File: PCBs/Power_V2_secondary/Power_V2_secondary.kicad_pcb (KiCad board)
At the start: 2 copper layers, 50.1 x 84.3 mm, 9 parts, among them IC7 ACS712ELCTR-20A-T, J1 PCIE-164-02-F-D-TH-TR, J15 YK4420203000G, J8 Conn_01x02, U2 178.6164.0001

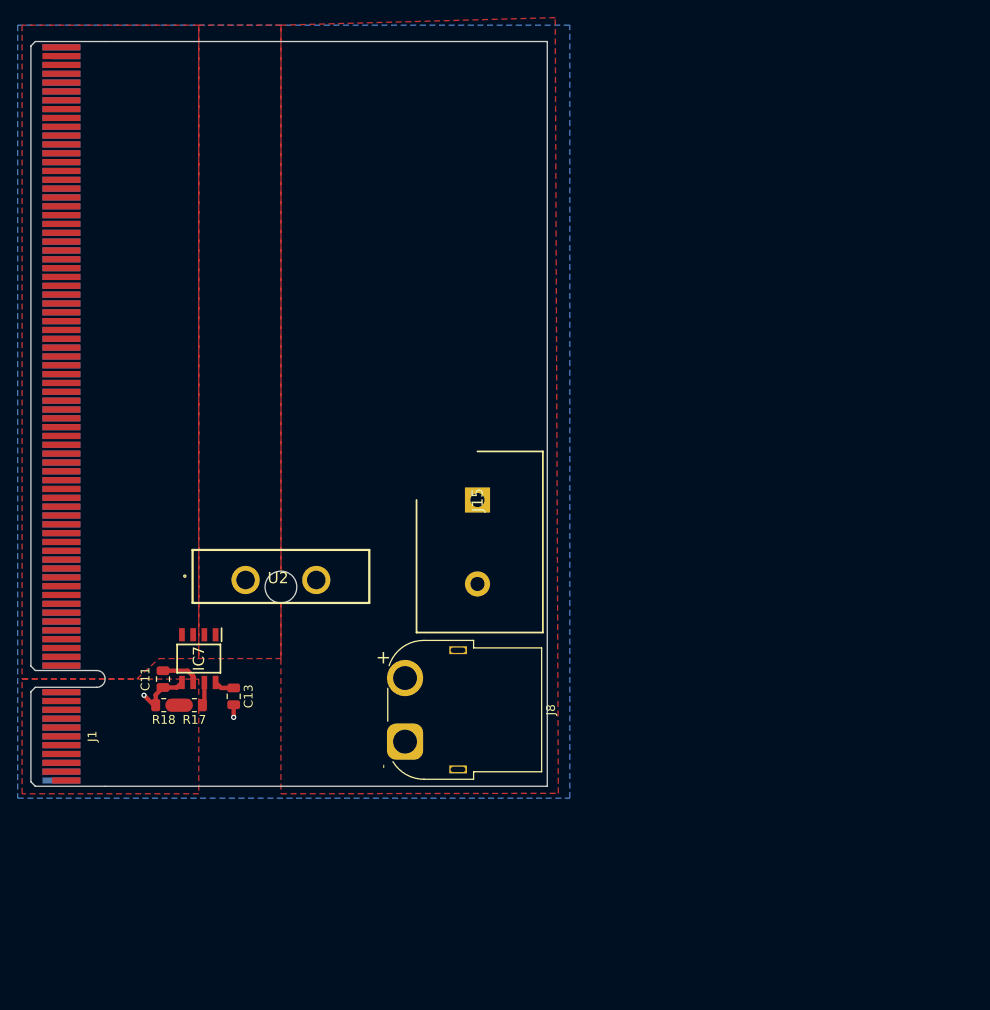
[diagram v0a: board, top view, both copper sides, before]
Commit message: finished secondary and beginning layout of main
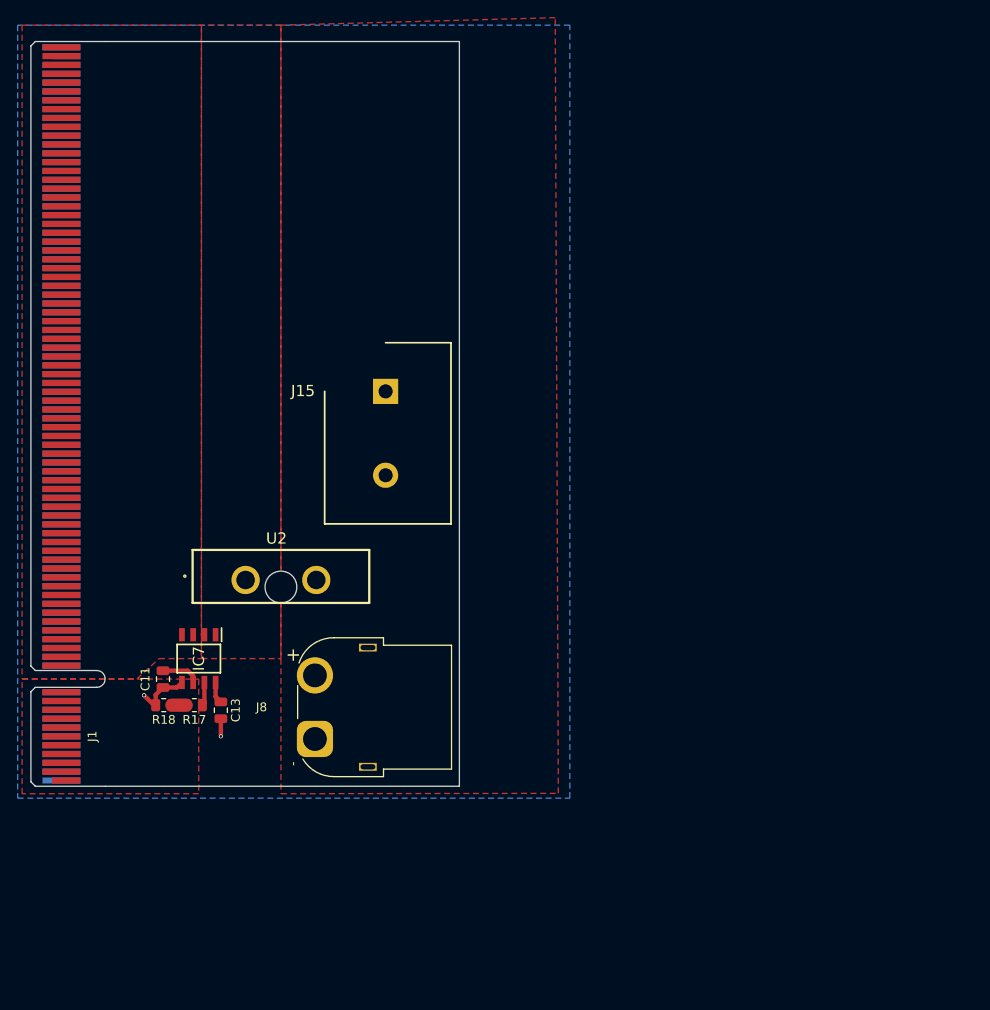
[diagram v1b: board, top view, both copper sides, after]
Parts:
- moved J15 16.1 mm to (81.7, 59.0)
- moved J8 10.2 mm to (73.7, 98.3)
- moved C13 2.14 mm to (63.0, 95.0)
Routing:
- net GND: track 7.94 -> 8.51 mm
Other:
- board size 50.1 x 84.3 mm -> 40.1 x 84.3 mm
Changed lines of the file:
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@@
 			(outputformat 1)
 			(mirror no)
-			(drillshape 1)
+			(drillshape 0)
 			(scaleselection 1)
-			(outputdirectory "")
+			(outputdirectory "./")
 		)
 	)
@@
 	(footprint "iprl_footprints:RHDR2W120P0X950_1X2_2050X1430X1790P"
 		(layer "F.Cu")
-		(at 92.05 71.25 -90)
+		(at 81.65 58.95 -90)
 		(descr "YK4420203000G")
 		(tags "Connector")
 		(property "Reference" "J15"
-			(at 0 0 90)
+			(at -0.05 9.35 0)
 			(layer "F.SilkS")
 			(effects
@@
 		)
 		(fp_text user "${REFERENCE}"
-			(at 0 0 90)
+			(at 0 9.35 0)
 			(layer "F.Fab")
 			(effects
@@
 		)
 		(embedded_fonts no)
-		(model "YK4420203000G.stp"
+		(model "/home/james/Documents/IPRL-Electronics-Hardware/PCBs/lib/models/YK4420203000G.stp"
 			(offset
 				(xyz 0 0 0)
@@
 	(footprint "Connector_AMASS:AMASS_XT60PW-F_1x02_P7.20mm_Horizontal"
 		(layer "F.Cu")
-		(at 83.85 98.6 -90)
+		(at 73.65 98.3 -90)
 		(descr "Connector XT60 Horizontal PCB Female, https://www.tme.eu/Document/1191bc2fa3aee3c446e5a895fd8f7983/XT60PW-F.pdf")
 		(tags "RC Connector XT60")
 		(property "Reference" "J8"
-			(at -3.6 -16.5 90)
+			(at -3.6 6.05 180)
 			(layer "F.SilkS")
 			(effects
@@
 	(footprint "Capacitor_SMD:C_0805_2012Metric"
 		(layer "F.Cu")
-		(at 64.45 93.47 -90)
+		(at 63 95.05 -90)
 		(descr "Capacitor SMD 0805 (2012 Metric), square (rectangular) end terminal, IPC-7351 nominal, (Body size source: IPC-SM-782 page 76, https://www.pcb-3d.com/wordpress/wp-content/uploads/ipc-sm-782a_amendment_1_and_2.pdf, https://docs.google.com/spreadsheets/d/1BsfQQcO9C6DZCsRaXUlFlo91Tg2WpOkGARC1WS5S8t0/edit?usp=sharing), generated with kicad-footprint-generator")
 		(tags "capacitor")
@@
 		(tags "Undefined or Miscellaneous")
 		(property "Reference" "U2"
-			(at -0.32439 -1.02275 0)
+			(at -0.5 -5.5 0)
 			(layer "F.SilkS")
 			(effects
@@
 		)
 		(fp_text user "${REFERENCE}"
-			(at -0.32439 -1.02275 0)
+			(at -0.4745 -5.5 0)
 			(layer "F.Fab")
 			(effects
@@
 		)
 		(embedded_fonts no)
-		(model "178.6164.0001.stp"
+		(model "${KIPRJMOD}/../lib/models/178.6164.0001.stp"
 			(offset
 				(xyz 4.999999925 10.31999954 -12.47000008)
@@
 		(tags "PCIe")
 		(property "Reference" "J1"
-			(at 5 3.5 -90)
+			(at 5 3.5 270)
 			(layer "F.SilkS")
 			(effects
@@
 		)
 		(property "Value" "PCIE-164-02-F-D-TH-TR"
-			(at 10.33 8.01 -90)
+			(at 10.33 8.01 270)
 			(layer "F.Fab")
 			(effects
@@
 		)
 		(fp_text user "${REFERENCE}"
-			(at 16 3.5 -90)
+			(at 16 3.5 270)
 			(layer "F.Fab")
 			(effects
@@
 	(gr_line
 		(start 49.9 103.65)
-		(end 99.95 103.65)
+		(end 90 103.65)
 		(stroke
 			(width 0.05)
@@
 	)
 	(gr_line
-		(start 99.95 103.65)
-		(end 99.95 19.35)
+		(start 90 103.65)
+		(end 90 19.35)
 		(stroke
 			(width 0.05)
@@
 	(gr_line
 		(start 49.9 19.35)
-		(end 99.95 19.35)
+		(end 90 19.35)
 		(stroke
 			(width 0.05)
@@
 	)
 	(segment
+		(start 63 96)
+		(end 63 98)
+		(width 0.5)
+		(layer "F.Cu")
+		(net 2)
+	)
+	(segment
 		(start 55.625 93.295)
 		(end 56.45 92.47)
@@
 		(net 2)
 	)
-	(segment
-		(start 64.45 94.42)
-		(end 64.45 95.85)
-		(width 0.5)
-		(layer "F.Cu")
-		(net 2)
-	)
 	(via
 		(at 54.3 93.35)
-		(size 0.6)
+		(size 0.45)
 		(drill 0.3)
 		(layers "F.Cu" "B.Cu")
@@
 	)
 	(via
-		(at 64.45 95.85)
-		(size 0.6)
+		(at 63 98)
+		(size 0.45)
 		(drill 0.3)
 		(layers "F.Cu" "B.Cu")
@@
 	)
 	(segment
-		(start 64.45 92.52)
-		(end 63.025 92.52)
+		(start 62.405 93.505)
+		(end 63 94.1)
 		(width 0.5)
 		(layer "F.Cu")
@@
 	)
 	(segment
-		(start 63.025 92.52)
-		(end 62.405 91.9)
+		(start 62.405 91.9)
+		(end 62.405 93.505)
 		(width 0.5)
 		(layer "F.Cu")
@@
 		(polygon
 			(pts
-				(xy 40.5 91.5) (xy 53.5 91.5) (xy 56 89.2) (xy 60.5 89.2) (xy 60.5 17.5) (xy 40.5 17.5)
+				(xy 40.5 91.5) (xy 53.5 91.5) (xy 56 89.2) (xy 60.8 89.2) (xy 60.8 17.5) (xy 40.5 17.5)
 			)
 		)
@@
 		(polygon
 			(pts
-				(xy 60.5 89.2) (xy 69.8 89.2) (xy 69.8 17.5) (xy 60.5 17.5)
+				(xy 60.8 89.2) (xy 69.8 89.2) (xy 69.8 17.5) (xy 60.8 17.5)
 			)
 		)
@@
 		(fill yes
 			(thermal_gap 0.5)
-			(thermal_bridge_width 0.5)
+			(thermal_bridge_width 1)
 		)
 		(polygon

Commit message: shortened main board and secondary
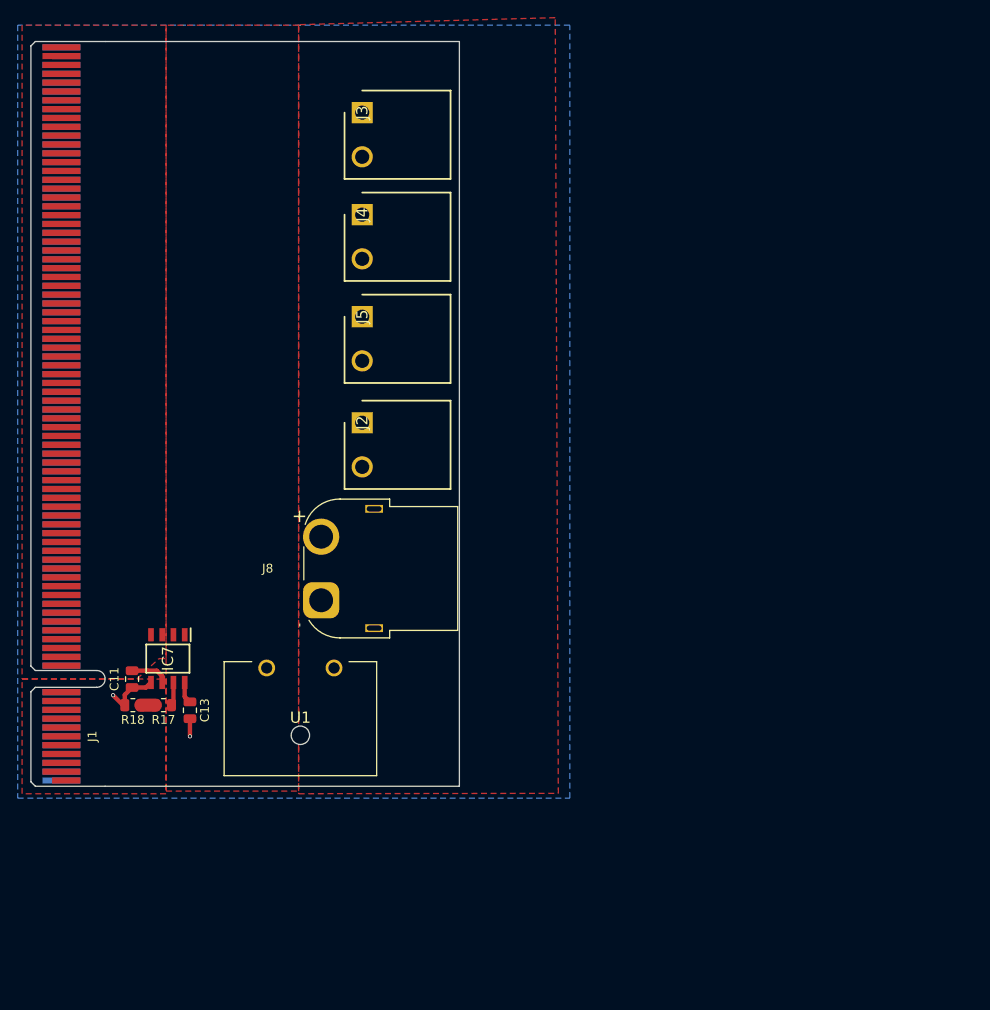
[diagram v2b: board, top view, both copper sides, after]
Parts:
- removed J15: YK4420203000G, iprl_footprints:RHDR2W120P0X950_1X2_2050X1430X1790P
- removed U2: 178.6164.0001, iprl_footprints:178.6164.XXX1
- added J2: 691312710002, iprl_footprints:SHDR2W100P0X500_1X2_1000X1200X850P, F.Cu at (79.0, 62.5)
- added J3: 691312710002, iprl_footprints:SHDR2W100P0X500_1X2_1000X1200X850P, F.Cu at (79.0, 27.4)
- added J4: 691312710002, iprl_footprints:SHDR2W100P0X500_1X2_1000X1200X850P, F.Cu at (79.0, 39.0)
- added J5: 691312710002, iprl_footprints:SHDR2W100P0X500_1X2_1000X1200X850P, F.Cu at (79.0, 50.5)
- added U1: 01530007Z, iprl_footprints:01530007Z, F.Cu at (72.0, 96.0)
- moved J8 15.7 mm to (74.3, 82.6)
- moved C11 3.50 mm to (53.0, 91.5)
- moved C13 3.50 mm to (59.5, 95.0)
- moved IC7 3.50 mm to (57.0, 89.2)
- moved R17 3.50 mm to (56.5, 94.5)
- moved R18 3.50 mm to (53.0, 94.5)

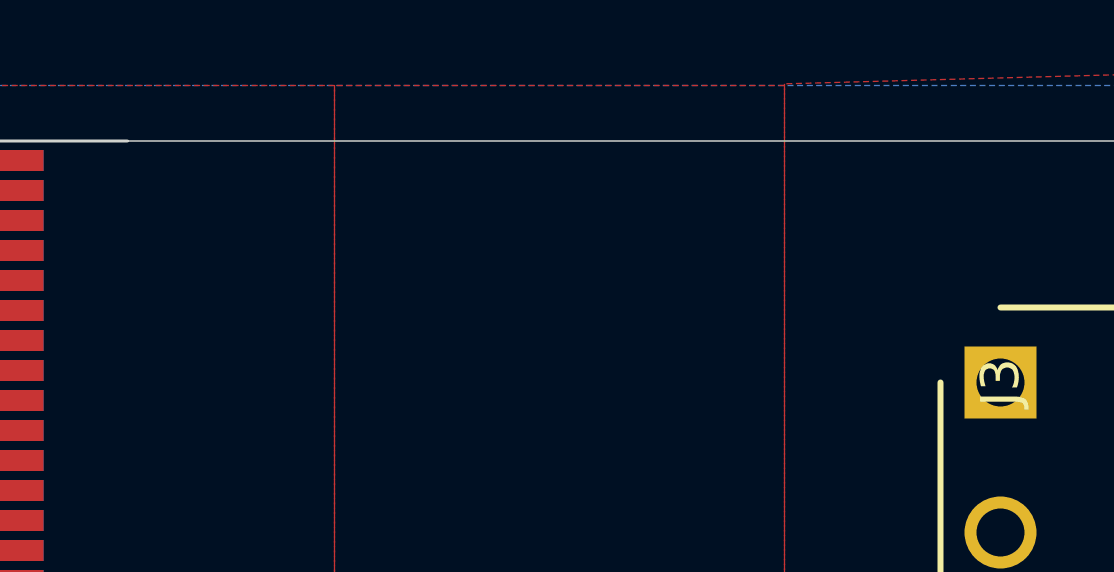
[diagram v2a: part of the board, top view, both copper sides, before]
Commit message: LEDs added to secondary
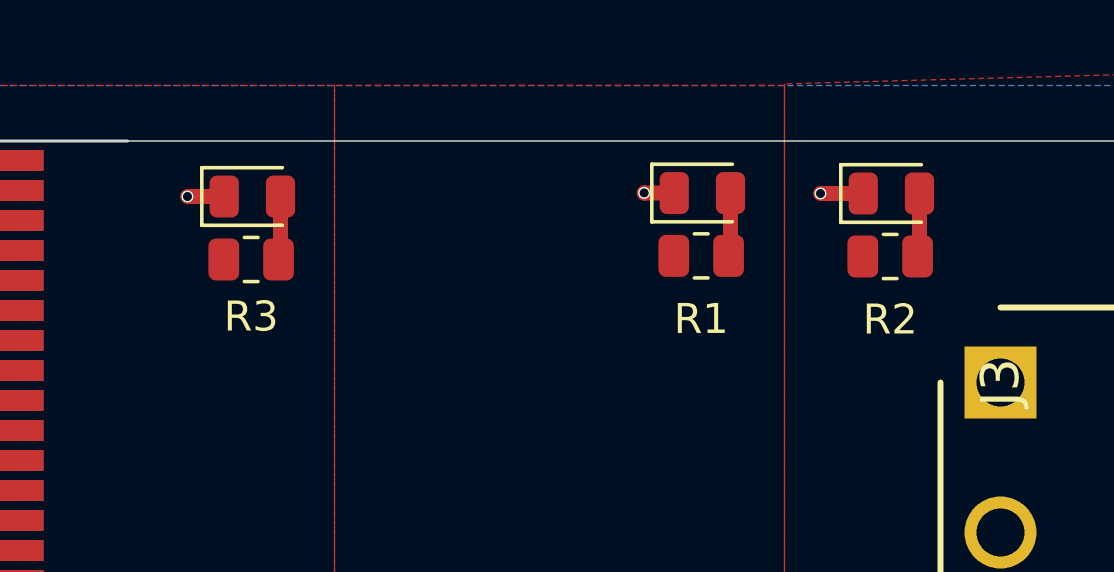
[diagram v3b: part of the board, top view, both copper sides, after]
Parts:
- added D1: LED, Diode_SMD:D_0805_2012Metric, F.Cu at (69.1, 21.1)
- added D2: LED, Diode_SMD:D_0805_2012Metric, F.Cu at (75.4, 21.1)
- added D3: LED, Diode_SMD:D_0805_2012Metric, F.Cu at (54.1, 21.2)
- added R1: 50k, Resistor_SMD:R_0805_2012Metric, F.Cu at (69.0, 23.2)
- added R2: 50k, Resistor_SMD:R_0805_2012Metric, F.Cu at (75.3, 23.2)
- added R3: 50k, Resistor_SMD:R_0805_2012Metric, F.Cu at (54.0, 23.3)
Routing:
- net GND: track 8.51 -> 12.2 mm, vias 2 -> 5
- net Net-(D3-A): track 0.00 -> 2.13 mm
- net Net-(D2-A): track 0.00 -> 2.13 mm
- net Net-(D1-A): track 0.00 -> 2.12 mm

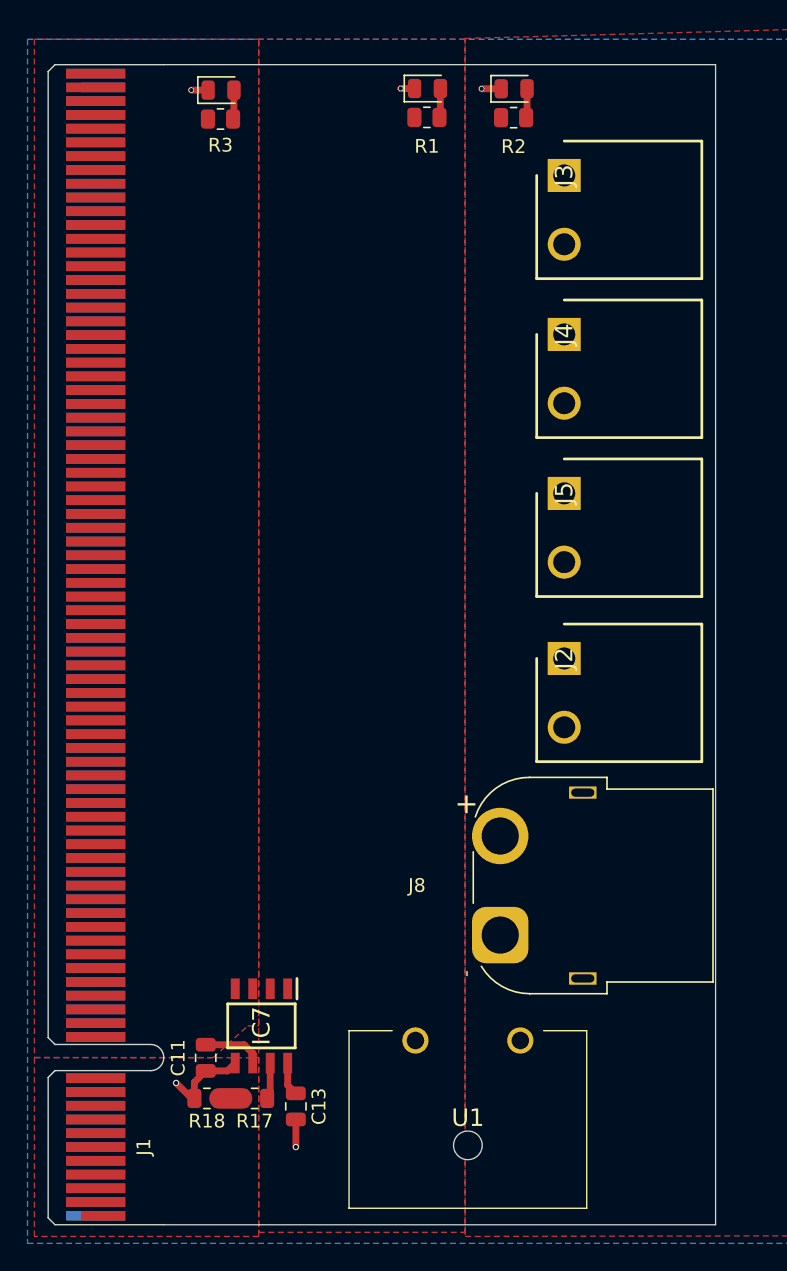
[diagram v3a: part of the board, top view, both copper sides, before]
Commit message: added LED indicators to board and redid power distribution in PCIe
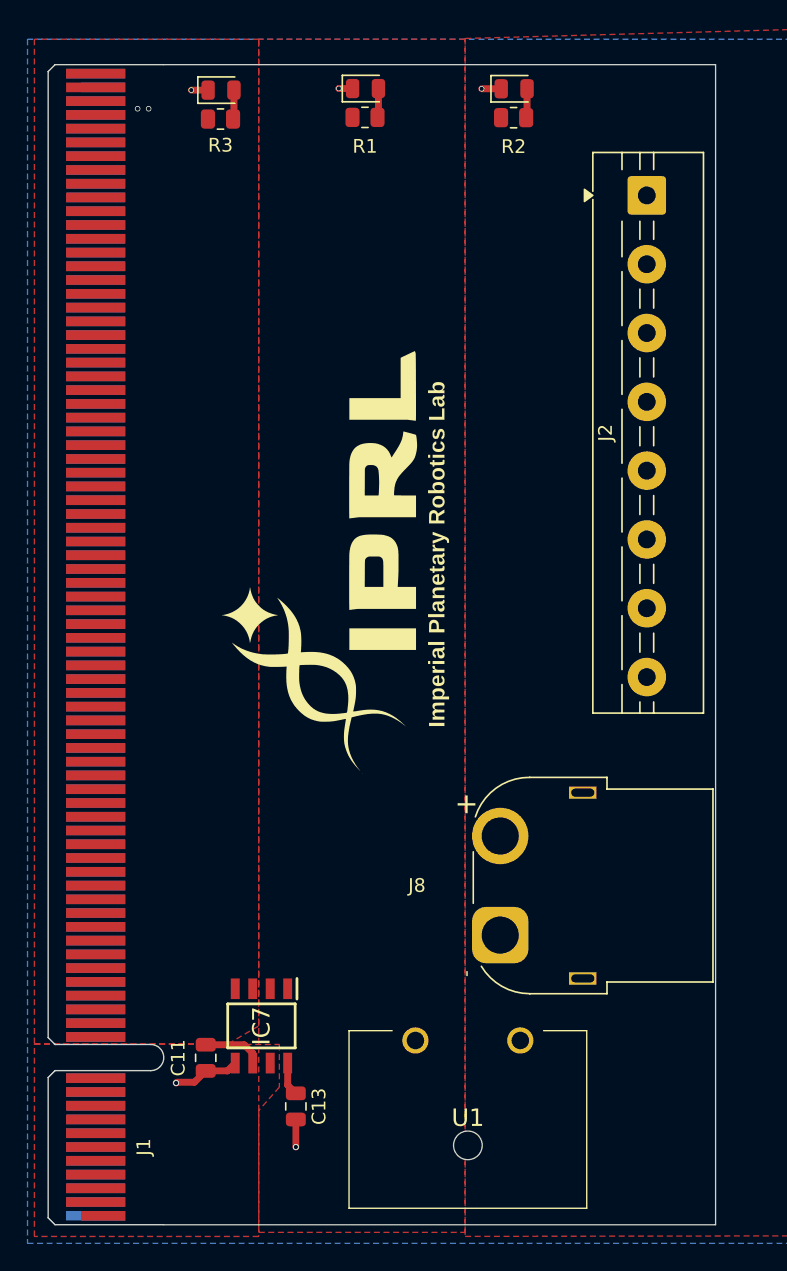
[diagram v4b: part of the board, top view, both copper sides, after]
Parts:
- removed J3, J4, J5: 691312710002, iprl_footprints:SHDR2W100P0X500_1X2_1000X1200X850P
- removed R17: 1k69, Resistor_SMD:R_0805_2012Metric
- removed R18: 4k7, Resistor_SMD:R_0805_2012Metric
- added G***: LOGO, main_lib:IPRL_31mm, F.Cu at (62.5, 55.4)
- J2: value 691312710002 -> Conn_01x08; footprint iprl_footprints:SHDR2W100P0X500_1X2_1000X1200X850P -> TerminalBlock:TerminalBlock_MaiXu_MX126-5.0-08P_1x08_P5.00mm
- moved J2 34.2 mm to (85.0, 28.9)
- moved D1 4.50 mm to (64.6, 21.1)
- moved R1 4.50 mm to (64.5, 23.2)
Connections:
- IC7 pad 7: /SYS_V -> /SYS_READ
- J1 pad A14: /14V8 -> GND
- J1 pad A15: /14V8 -> GND
- J1 pad A18: /14V8 -> GND
- J1 pad A19: /14V8 -> GND
- J1 pad A22: /14V8 -> GND
- J1 pad A23: /14V8 -> GND
- J1 pad A26: /14V8 -> GND
- J1 pad A27: /14V8 -> GND
- J1 pad A30: /14V8 -> GND
- J1 pad A31: /14V8 -> GND
- J1 pad A34: /14V8 -> GND
- J1 pad A35: /14V8 -> GND
- J1 pad A38: /14V8 -> GND
- J1 pad A39: /14V8 -> GND
- J1 pad A42: /14V8 -> GND
- J1 pad A43: /14V8 -> GND
- J1 pad A46: /14V8 -> GND
- J1 pad A47: /14V8 -> GND
- J1 pad A50: /14V8 -> GND
- J1 pad A51: /14V8 -> GND
- J1 pad A54: /14V8 -> GND
- J1 pad A55: /14V8 -> GND
- J1 pad A58: /14V8 -> GND
- J1 pad A59: /14V8 -> GND
- J1 pad A62: /14V8 -> GND
- J1 pad A63: /14V8 -> GND
- J1 pad A66: /14V8 -> GND
- J1 pad A67: /14V8 -> GND
- J1 pad A70: /14V8 -> GND
- J1 pad A71: /14V8 -> GND
- J1 pad A74: /14V8 -> GND
- J1 pad A75: /14V8 -> GND
- J1 pad A78: /14V8 -> GND
- J1 pad A79: /14V8 -> GND
- J1 pad A82: /14V8 -> GND
- J1 pad B1: GND -> Net-(J1-PadB1)
- J1 pad B10: GND -> Net-(J1-PadB1)
- J1 pad B11: GND -> Net-(J1-PadB1)
- J1 pad B12: GND -> /14V8
- J1 pad B15: GND -> /14V8
- J1 pad B16: GND -> /14V8
- J1 pad B19: GND -> /14V8
- J1 pad B2: GND -> Net-(J1-PadB1)
- J1 pad B20: GND -> /14V8
- J1 pad B23: GND -> /14V8
- J1 pad B24: GND -> /14V8
- J1 pad B27: GND -> /14V8
- J1 pad B28: GND -> /14V8
- J1 pad B3: GND -> Net-(J1-PadB1)
- J1 pad B31: GND -> /14V8
- J1 pad B32: GND -> /14V8
- J1 pad B35: GND -> /14V8
- J1 pad B36: GND -> /14V8
- J1 pad B39: GND -> /14V8
- J1 pad B4: GND -> Net-(J1-PadB1)
- J1 pad B40: GND -> /14V8
- J1 pad B43: GND -> /14V8
- J1 pad B44: GND -> /14V8
- J1 pad B47: GND -> /14V8
- J1 pad B48: GND -> /14V8
- J1 pad B5: GND -> Net-(J1-PadB1)
- J1 pad B51: GND -> /14V8
- J1 pad B52: GND -> /14V8
- J1 pad B55: GND -> /14V8
- J1 pad B56: GND -> /14V8
- J1 pad B59: GND -> /14V8
- J1 pad B6: GND -> Net-(J1-PadB1)
- J1 pad B60: GND -> /14V8
- J1 pad B63: GND -> /14V8
- J1 pad B64: GND -> /14V8
- J1 pad B67: GND -> /14V8
- J1 pad B68: GND -> /14V8
- J1 pad B7: GND -> Net-(J1-PadB1)
- J1 pad B71: GND -> /14V8
- J1 pad B72: GND -> /14V8
- J1 pad B75: GND -> /14V8
- J1 pad B76: GND -> /14V8
- J1 pad B79: GND -> /14V8
- J1 pad B8: GND -> Net-(J1-PadB1)
- J1 pad B80: GND -> /14V8
- J1 pad B9: GND -> Net-(J1-PadB1)
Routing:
- net /SYS_V: track 2.66 -> 0.00 mm
- net /SYS_READ: track 1.64 -> 0.00 mm
- net GND: track 12.2 -> 10.6 mm
- net /14V8: vias 0 -> 2
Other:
- board text added: "POWER BOARD: SECONDARY"
